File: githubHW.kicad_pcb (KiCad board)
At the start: 2 copper layers, 100.1 x 99.6 mm, 142 parts, among them J1 Conn_01x06, J2 Conn_01x07, J3 Conn_01x07, J4 Conn_01x07, J5 Conn_01x07, J6 Conn_01x06, SW1 SW_Push, SW2 SW_Push, SW3 SW_Push, SW4 SW_Push, U1 WeMos_mini, U2 TPIC6B595N, U3 TLC5940NT, U4 TPIC6B595N

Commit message: connection issue fixed
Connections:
- U4 pad 14: Net-(D101-Pad1) -> Net-(D103-Pad1)
- U4 pad 15: Net-(D100-Pad1) -> Net-(D104-Pad1)
- U4 pad 16: Net-(D106-Pad1) -> Net-(D105-Pad1)
- U4 pad 4: Net-(D105-Pad1) -> Net-(D106-Pad1)
- U4 pad 5: Net-(D104-Pad1) -> Net-(D100-Pad1)
- U4 pad 6: Net-(D103-Pad1) -> Net-(D101-Pad1)
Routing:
- net Net-(D103-Pad1): track 244.8 -> 271.5 mm
- net Net-(D104-Pad1): track 236.5 -> 260.0 mm
- net Net-(D105-Pad1): track 233.9 -> 255.1 mm
- net Net-(D101-Pad1): track 272.0 -> 257.5 mm
- net Net-(D100-Pad1): track 272.7 -> 259.0 mm
- net Net-(D106-Pad1): track 270.2 -> 257.5 mm
- net Net-(D100-Pad2): track 60.9 -> 62.7 mm
- net Net-(D92-Pad2): track 58.8 -> 60.5 mm

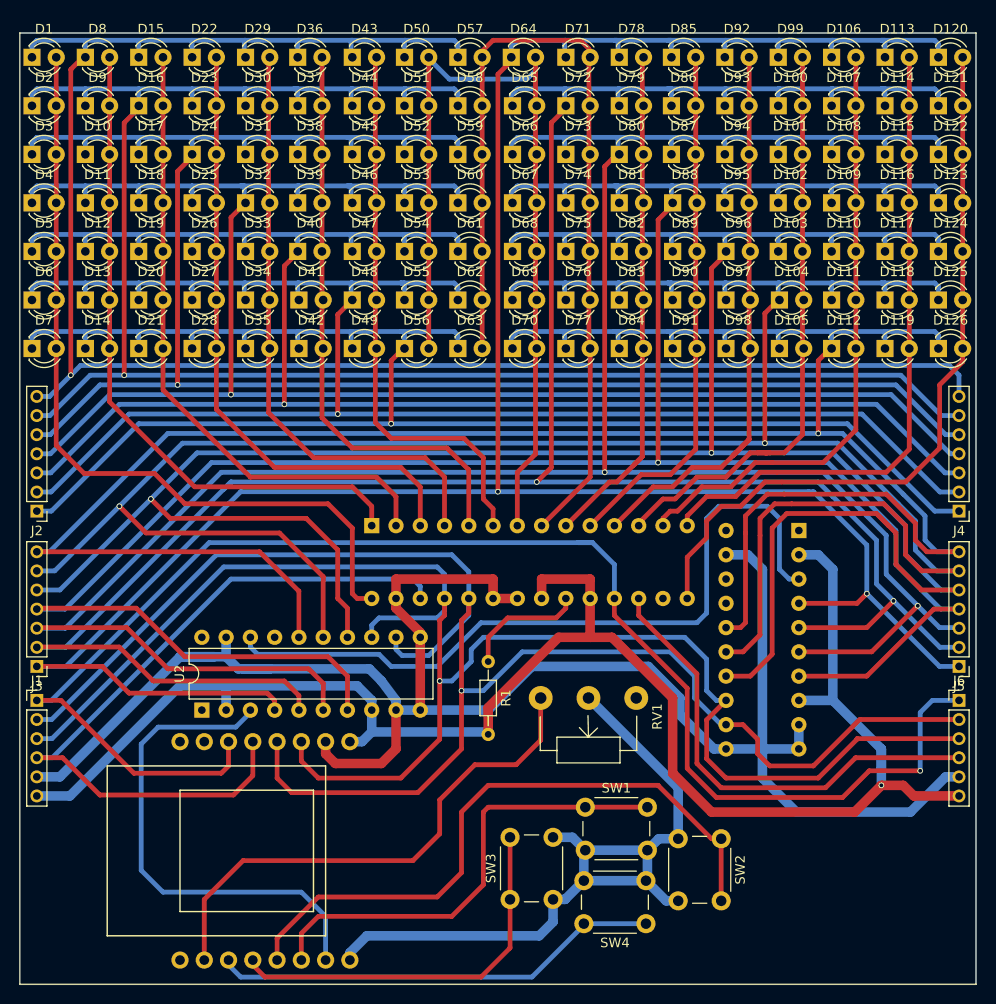
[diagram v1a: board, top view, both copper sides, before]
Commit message: buttons connection changed
now using WeMos' pullups
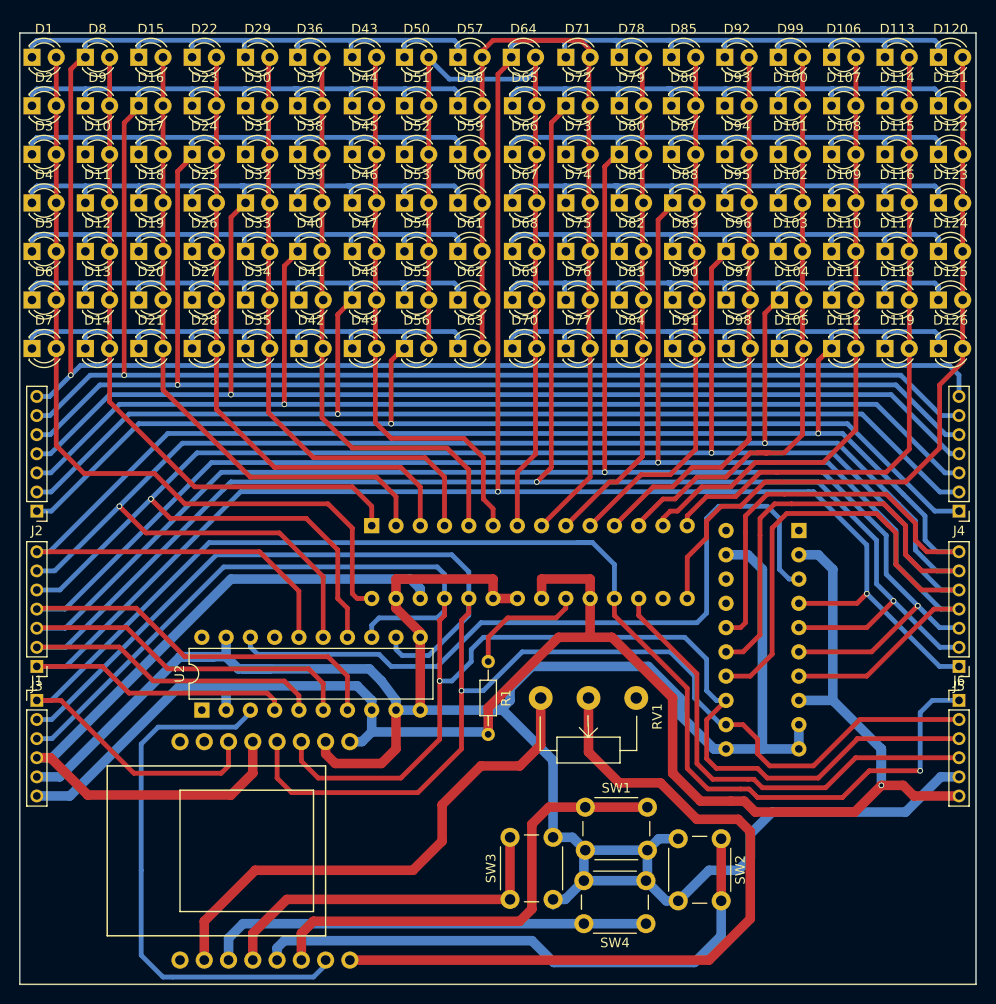
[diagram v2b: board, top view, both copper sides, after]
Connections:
- SW1 pad 2: /3.3V -> GND
- SW2 pad 2: /3.3V -> GND
- SW3 pad 2: /3.3V -> GND
- SW4 pad 2: /3.3V -> GND
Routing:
- net GND: track 198.8 -> 263.8 mm
- net Net-(SW2-Pad1): track 67.9 -> 60.3 mm
- net Net-(U1-Pad15): track 52.6 -> 56.9 mm
- net Net-(SW3-Pad1): track 40.8 -> 37.7 mm
- net /3.3V: track 81.9 -> 78.9 mm
- net Net-(RV1-Pad3): track 55.0 -> 54.1 mm
- net Net-(SW1-Pad1): track 48.9 -> 49.7 mm

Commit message: Revert "connection issue fixed"
This reverts commit d7eb6beb1c8d570a5e8c06e88c024579e6cb722b.
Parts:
- U4: moved to F.Cu
- moved U4 23.5 mm to (183.0, 150.2)
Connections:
- U4 pad 14: Net-(D103-Pad1) -> Net-(D10-Pad1)
- U4 pad 15: Net-(D104-Pad1) -> Net-(D16-Pad1)
- U4 pad 16: Net-(D105-Pad1) -> Net-(D1-Pad1)
- U4 pad 4: Net-(D106-Pad1) -> Net-(D14-Pad1)
- U4 pad 5: Net-(D100-Pad1) -> Net-(D13-Pad1)
- U4 pad 6: Net-(D101-Pad1) -> Net-(D12-Pad1)
- U4 pad 7: Net-(D102-Pad1) -> Net-(D11-Pad1)
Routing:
- net Net-(D103-Pad1): track 271.5 -> 224.6 mm
- net Net-(D1-Pad1): track 195.9 -> 240.9 mm
- net Net-(D104-Pad1): track 260.0 -> 216.8 mm
- net Net-(D105-Pad1): track 255.1 -> 213.6 mm
- net Net-(D16-Pad1): track 190.0 -> 230.5 mm
- net Net-(D10-Pad1): track 187.4 -> 219.9 mm
- net Net-(D14-Pad1): track 173.4 -> 198.3 mm
- net Net-(D13-Pad1): track 176.7 -> 201.6 mm
- net Net-(D12-Pad1): track 180.1 -> 204.6 mm
- net Net-(D11-Pad1): track 184.1 -> 207.4 mm
- net /M_CLK: track 172.5 -> 193.5 mm, vias 1 -> 3
- net Net-(D102-Pad1): track 260.3 -> 240.0 mm
- net Net-(D101-Pad1): track 257.5 -> 242.2 mm, vias 2 -> 1
- net /LATCH: track 174.0 -> 188.5 mm, vias 1 -> 4
- net Net-(D100-Pad1): track 259.0 -> 246.8 mm, vias 2 -> 1
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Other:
- net class Default: clearance 0.25 -> 0.3
- rule trace_clearance: 0.25 -> 0.3

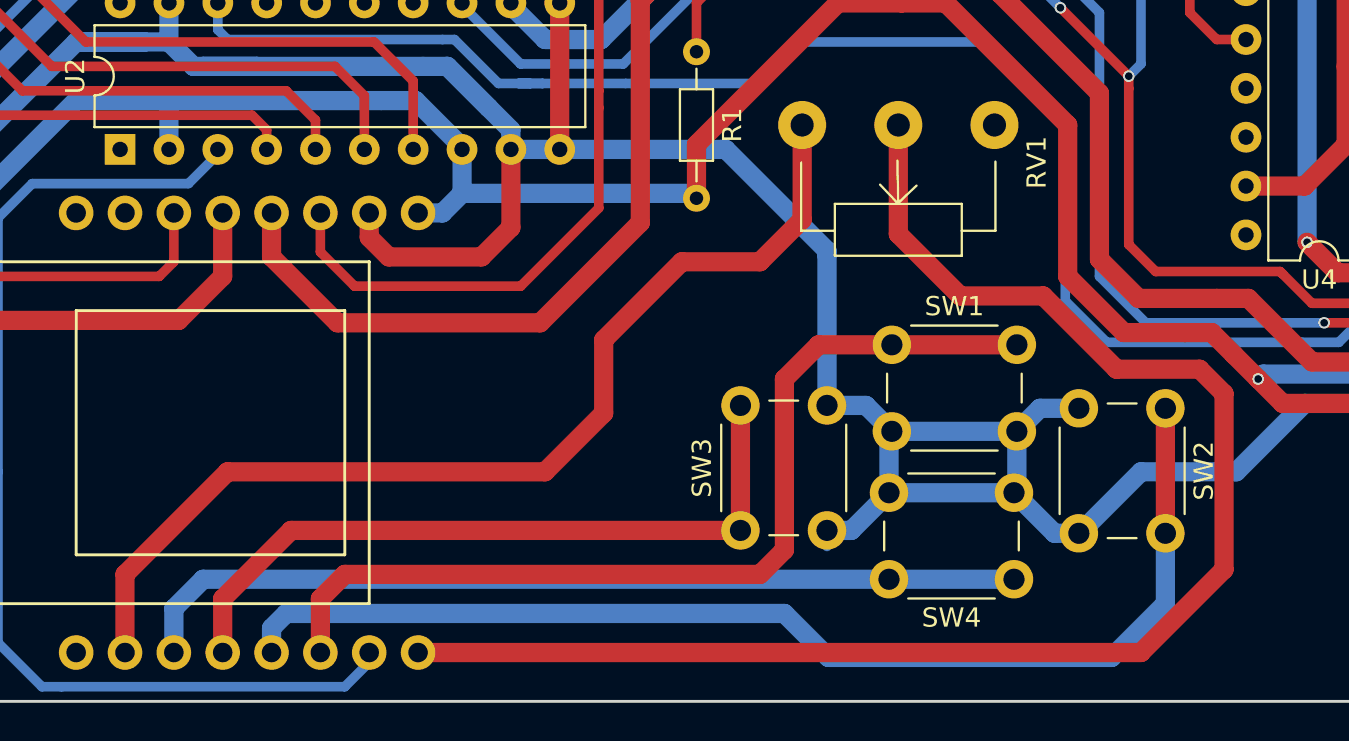
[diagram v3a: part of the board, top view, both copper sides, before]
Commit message: poti connection corrected
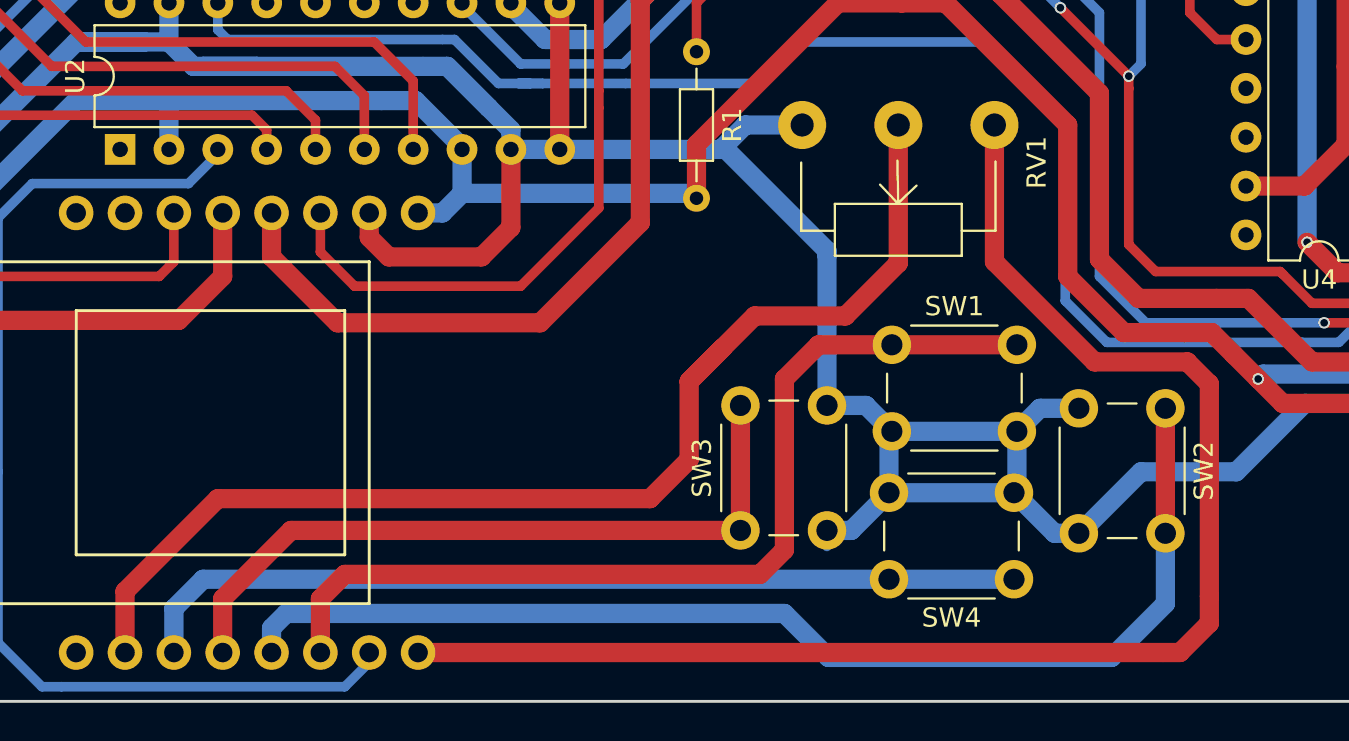
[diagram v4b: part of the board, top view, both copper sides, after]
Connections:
- RV1 pad 1: Net-(RV1-Pad1) -> /3.3V
- RV1 pad 2: /3.3V -> Net-(RV1-Pad2)
- RV1 pad 3: Net-(RV1-Pad3) -> GND
- U1 pad 10: Net-(RV1-Pad3) -> Net-(RV1-Pad2)
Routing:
- net Net-(RV1-Pad2): track 0.00 -> 63.0 mm
- net Net-(RV1-Pad3): track 54.1 -> 0.00 mm
- net GND: track 263.1 -> 267.9 mm
- net /3.3V: track 78.9 -> 75.1 mm

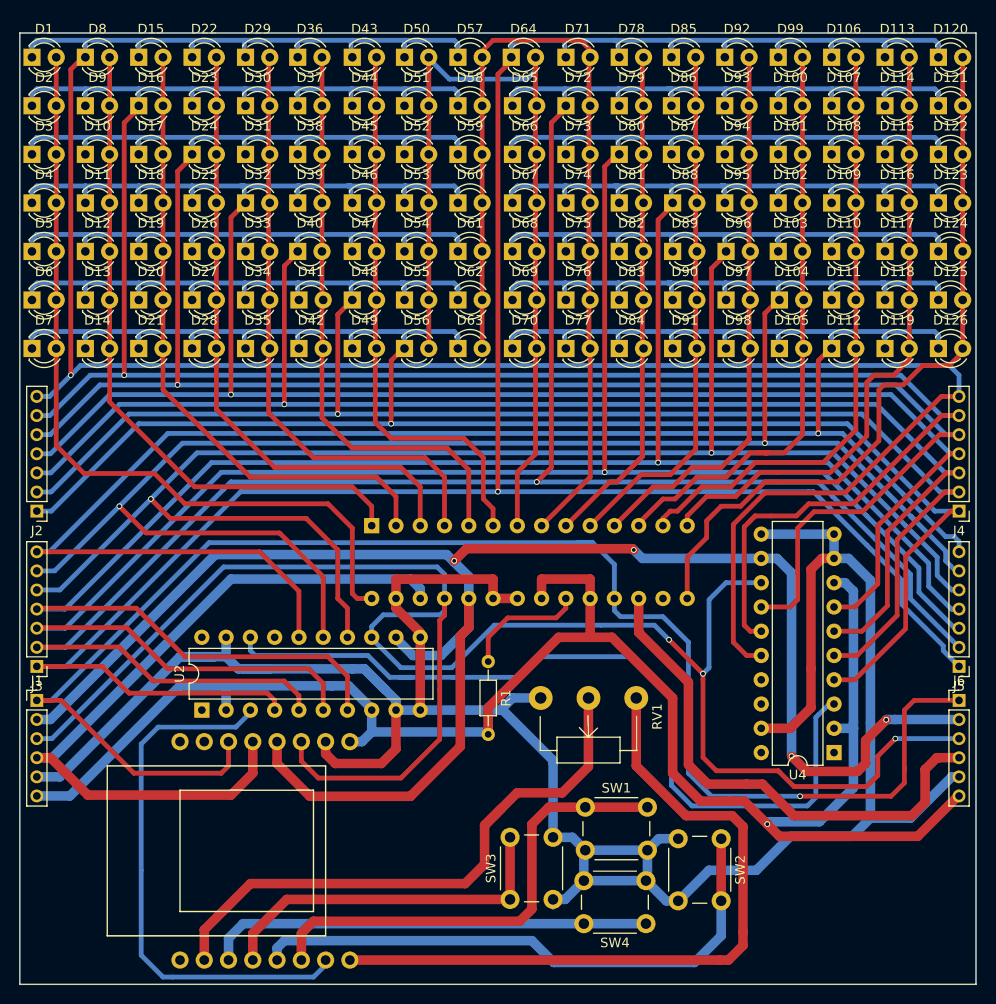
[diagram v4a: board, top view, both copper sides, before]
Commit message: wemos files commited for better usability.
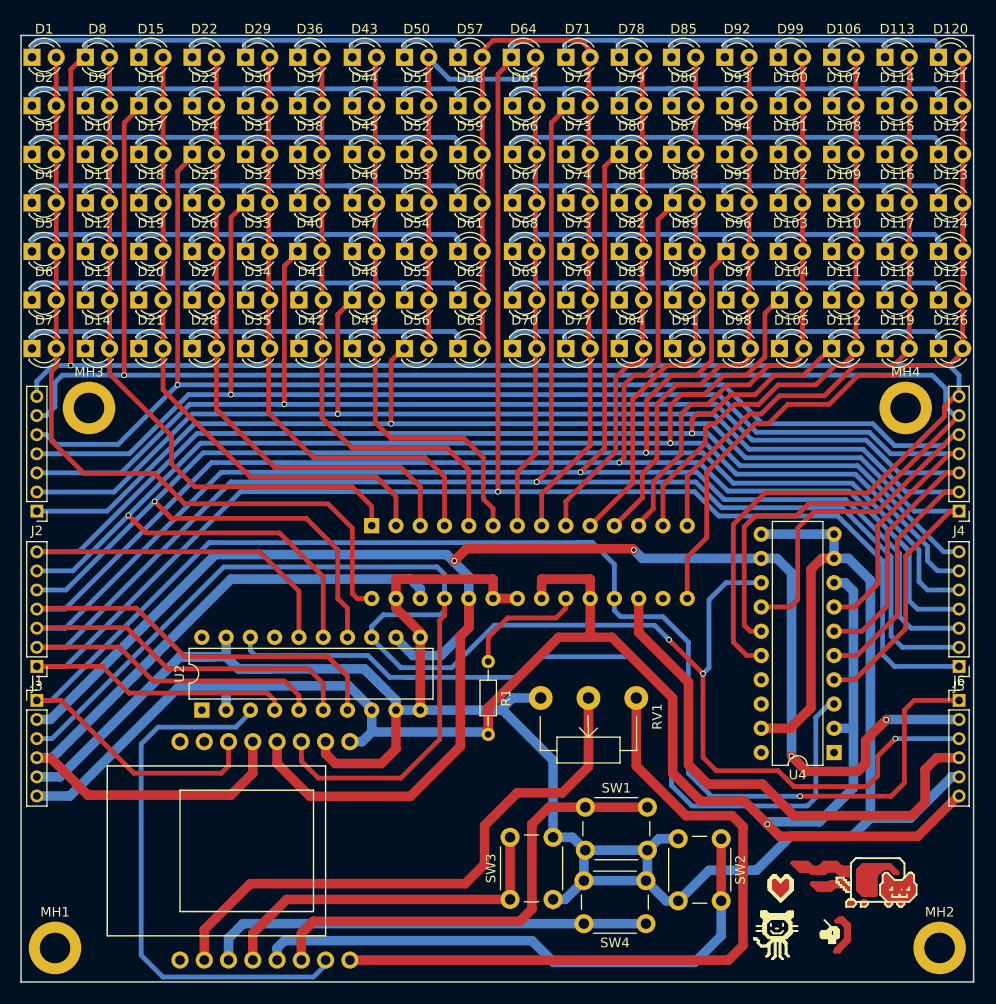
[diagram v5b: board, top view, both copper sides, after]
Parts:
- added MH1: MOUNTHOLE, Mounting_Holes:MountingHole_3.2mm_M3_ISO14580_Pad, F.Cu at (101.5, 170.7)
- added MH2: MOUNTHOLE, Mounting_Holes:MountingHole_3.2mm_M3_ISO14580_Pad, F.Cu at (194.1, 170.7)
- added MH3: MOUNTHOLE, Mounting_Holes:MountingHole_3.2mm_M3_ISO14580_Pad, F.Cu at (105.0, 114.2)
- added MH4: MOUNTHOLE, Mounting_Holes:MountingHole_3.2mm_M3_ISO14580_Pad, F.Cu at (190.5, 114.2)
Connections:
- D1 pad 1: Net-(D1-Pad1) -> Net-
- D1 pad 2: Net-(D1-Pad2) -> Net-
- D10 pad 1: Net-(D10-Pad1) -> Net-
- D10 pad 2: Net-(D10-Pad2) -> Net-
- D100 pad 1: Net-(D100-Pad1) -> Net-
- D100 pad 2: Net-(D100-Pad2) -> Net-
- D101 pad 1: Net-(D101-Pad1) -> Net-
- D101 pad 2: Net-(D100-Pad2) -> Net-
- D102 pad 1: Net-(D102-Pad1) -> Net-
- D102 pad 2: Net-(D100-Pad2) -> Net-
- D103 pad 1: Net-(D103-Pad1) -> Net-
- D103 pad 2: Net-(D100-Pad2) -> Net-
- D104 pad 1: Net-(D104-Pad1) -> Net-
- D104 pad 2: Net-(D100-Pad2) -> Net-
- D105 pad 1: Net-(D105-Pad1) -> Net-
- D105 pad 2: Net-(D100-Pad2) -> Net-
- D106 pad 1: Net-(D106-Pad1) -> Net-
- D106 pad 2: Net-(D106-Pad2) -> Net-
- D107 pad 1: Net-(D100-Pad1) -> Net-
- D107 pad 2: Net-(D106-Pad2) -> Net-
- D108 pad 1: Net-(D101-Pad1) -> Net-
- D108 pad 2: Net-(D106-Pad2) -> Net-
- D109 pad 1: Net-(D102-Pad1) -> Net-
- D109 pad 2: Net-(D106-Pad2) -> Net-
- D11 pad 1: Net-(D11-Pad1) -> Net-
- D11 pad 2: Net-(D10-Pad2) -> Net-
- D110 pad 1: Net-(D103-Pad1) -> Net-
- D110 pad 2: Net-(D106-Pad2) -> Net-
- D111 pad 1: Net-(D104-Pad1) -> Net-
- D111 pad 2: Net-(D106-Pad2) -> Net-
- D112 pad 1: Net-(D105-Pad1) -> Net-
- D112 pad 2: Net-(D106-Pad2) -> Net-
- D113 pad 1: Net-(D106-Pad1) -> Net-
- D113 pad 2: Net-(D113-Pad2) -> Net-
- D114 pad 1: Net-(D100-Pad1) -> Net-
- D114 pad 2: Net-(D113-Pad2) -> Net-
- D115 pad 1: Net-(D101-Pad1) -> Net-
- D115 pad 2: Net-(D113-Pad2) -> Net-
- D116 pad 1: Net-(D102-Pad1) -> Net-
- D116 pad 2: Net-(D113-Pad2) -> Net-
- D117 pad 1: Net-(D103-Pad1) -> Net-
- D117 pad 2: Net-(D113-Pad2) -> Net-
- D118 pad 1: Net-(D104-Pad1) -> Net-
- D118 pad 2: Net-(D113-Pad2) -> Net-
- D119 pad 1: Net-(D105-Pad1) -> Net-
- D119 pad 2: Net-(D113-Pad2) -> Net-
- D12 pad 1: Net-(D12-Pad1) -> Net-
- D12 pad 2: Net-(D10-Pad2) -> Net-
- D120 pad 1: Net-(D106-Pad1) -> Net-
- D120 pad 2: Net-(D120-Pad2) -> Net-
- D121 pad 1: Net-(D100-Pad1) -> Net-
- D121 pad 2: Net-(D120-Pad2) -> Net-
- D122 pad 1: Net-(D101-Pad1) -> Net-
- D122 pad 2: Net-(D120-Pad2) -> Net-
- D123 pad 1: Net-(D102-Pad1) -> Net-
- D123 pad 2: Net-(D120-Pad2) -> Net-
- D124 pad 1: Net-(D103-Pad1) -> Net-
- D124 pad 2: Net-(D120-Pad2) -> Net-
- D125 pad 1: Net-(D104-Pad1) -> Net-
- D125 pad 2: Net-(D120-Pad2) -> Net-
- D126 pad 1: Net-(D105-Pad1) -> Net-
- D126 pad 2: Net-(D120-Pad2) -> Net-
- D13 pad 1: Net-(D13-Pad1) -> Net-
- D13 pad 2: Net-(D10-Pad2) -> Net-
- D14 pad 1: Net-(D14-Pad1) -> Net-
- D14 pad 2: Net-(D10-Pad2) -> Net-
- D15 pad 1: Net-(D1-Pad1) -> Net-
- D15 pad 2: Net-(D15-Pad2) -> Net-
- D16 pad 1: Net-(D16-Pad1) -> Net-
- D16 pad 2: Net-(D15-Pad2) -> Net-
- D17 pad 1: Net-(D10-Pad1) -> Net-
- D17 pad 2: Net-(D15-Pad2) -> Net-
- D18 pad 1: Net-(D11-Pad1) -> Net-
- D18 pad 2: Net-(D15-Pad2) -> Net-
- D19 pad 1: Net-(D12-Pad1) -> Net-
- D19 pad 2: Net-(D15-Pad2) -> Net-
- D2 pad 1: Net-(D16-Pad1) -> Net-
- D2 pad 2: Net-(D1-Pad2) -> Net-
- D20 pad 1: Net-(D13-Pad1) -> Net-
- D20 pad 2: Net-(D15-Pad2) -> Net-
- D21 pad 1: Net-(D14-Pad1) -> Net-
- D21 pad 2: Net-(D15-Pad2) -> Net-
- D22 pad 1: Net-(D1-Pad1) -> Net-
- D22 pad 2: Net-(D22-Pad2) -> Net-
- D23 pad 1: Net-(D16-Pad1) -> Net-
- D23 pad 2: Net-(D22-Pad2) -> Net-
- D24 pad 1: Net-(D10-Pad1) -> Net-
- D24 pad 2: Net-(D22-Pad2) -> Net-
- D25 pad 1: Net-(D11-Pad1) -> Net-
- D25 pad 2: Net-(D22-Pad2) -> Net-
- D26 pad 1: Net-(D12-Pad1) -> Net-
- D26 pad 2: Net-(D22-Pad2) -> Net-
- D27 pad 1: Net-(D13-Pad1) -> Net-
- D27 pad 2: Net-(D22-Pad2) -> Net-
- D28 pad 1: Net-(D14-Pad1) -> Net-
- D28 pad 2: Net-(D22-Pad2) -> Net-
- D29 pad 1: Net-(D1-Pad1) -> Net-
- D29 pad 2: Net-(D29-Pad2) -> Net-
- D3 pad 1: Net-(D10-Pad1) -> Net-
- D3 pad 2: Net-(D1-Pad2) -> Net-
- D30 pad 1: Net-(D16-Pad1) -> Net-
- D30 pad 2: Net-(D29-Pad2) -> Net-
- D31 pad 1: Net-(D10-Pad1) -> Net-
- D31 pad 2: Net-(D29-Pad2) -> Net-
- D32 pad 1: Net-(D11-Pad1) -> Net-
- D32 pad 2: Net-(D29-Pad2) -> Net-
- D33 pad 1: Net-(D12-Pad1) -> Net-
- D33 pad 2: Net-(D29-Pad2) -> Net-
- D34 pad 1: Net-(D13-Pad1) -> Net-
- D34 pad 2: Net-(D29-Pad2) -> Net-
- D35 pad 1: Net-(D14-Pad1) -> Net-
- D35 pad 2: Net-(D29-Pad2) -> Net-
- D36 pad 1: Net-(D1-Pad1) -> Net-
- D36 pad 2: Net-(D36-Pad2) -> Net-
- D37 pad 1: Net-(D16-Pad1) -> Net-
- D37 pad 2: Net-(D36-Pad2) -> Net-
- D38 pad 1: Net-(D10-Pad1) -> Net-
- D38 pad 2: Net-(D36-Pad2) -> Net-
- D39 pad 1: Net-(D11-Pad1) -> Net-
- D39 pad 2: Net-(D36-Pad2) -> Net-
- D4 pad 1: Net-(D11-Pad1) -> Net-
- D4 pad 2: Net-(D1-Pad2) -> Net-
- D40 pad 1: Net-(D12-Pad1) -> Net-
- D40 pad 2: Net-(D36-Pad2) -> Net-
- D41 pad 1: Net-(D13-Pad1) -> Net-
- D41 pad 2: Net-(D36-Pad2) -> Net-
- D42 pad 1: Net-(D14-Pad1) -> Net-
- D42 pad 2: Net-(D36-Pad2) -> Net-
- D43 pad 1: Net-(D1-Pad1) -> Net-
- D43 pad 2: Net-(D43-Pad2) -> Net-
- D44 pad 1: Net-(D16-Pad1) -> Net-
- D44 pad 2: Net-(D43-Pad2) -> Net-
- D45 pad 1: Net-(D10-Pad1) -> Net-
- D45 pad 2: Net-(D43-Pad2) -> Net-
- D46 pad 1: Net-(D11-Pad1) -> Net-
- D46 pad 2: Net-(D43-Pad2) -> Net-
- D47 pad 1: Net-(D12-Pad1) -> Net-
- D47 pad 2: Net-(D43-Pad2) -> Net-
- D48 pad 1: Net-(D13-Pad1) -> Net-
- D48 pad 2: Net-(D43-Pad2) -> Net-
- D49 pad 1: Net-(D14-Pad1) -> Net-
- D49 pad 2: Net-(D43-Pad2) -> Net-
- D5 pad 1: Net-(D12-Pad1) -> Net-
- D5 pad 2: Net-(D1-Pad2) -> Net-
- D50 pad 1: Net-(D1-Pad1) -> Net-
- D50 pad 2: Net-(D50-Pad2) -> Net-
- D51 pad 1: Net-(D16-Pad1) -> Net-
- D51 pad 2: Net-(D50-Pad2) -> Net-
- D52 pad 1: Net-(D10-Pad1) -> Net-
- D52 pad 2: Net-(D50-Pad2) -> Net-
- D53 pad 1: Net-(D11-Pad1) -> Net-
- D53 pad 2: Net-(D50-Pad2) -> Net-
- D54 pad 1: Net-(D12-Pad1) -> Net-
- D54 pad 2: Net-(D50-Pad2) -> Net-
- D55 pad 1: Net-(D13-Pad1) -> Net-
- D55 pad 2: Net-(D50-Pad2) -> Net-
- D56 pad 1: Net-(D14-Pad1) -> Net-
- D56 pad 2: Net-(D50-Pad2) -> Net-
- D57 pad 1: Net-(D1-Pad1) -> Net-
- D57 pad 2: Net-(D57-Pad2) -> Net-
- D58 pad 1: Net-(D16-Pad1) -> Net-
- D58 pad 2: Net-(D57-Pad2) -> Net-
- D59 pad 1: Net-(D10-Pad1) -> Net-
- D59 pad 2: Net-(D57-Pad2) -> Net-
- D6 pad 1: Net-(D13-Pad1) -> Net-
- D6 pad 2: Net-(D1-Pad2) -> Net-
- D60 pad 1: Net-(D11-Pad1) -> Net-
- D60 pad 2: Net-(D57-Pad2) -> Net-
- D61 pad 1: Net-(D12-Pad1) -> Net-
- D61 pad 2: Net-(D57-Pad2) -> Net-
- D62 pad 1: Net-(D13-Pad1) -> Net-
- D62 pad 2: Net-(D57-Pad2) -> Net-
- D63 pad 1: Net-(D14-Pad1) -> Net-
- D63 pad 2: Net-(D57-Pad2) -> Net-
- D64 pad 1: Net-(D106-Pad1) -> Net-
- D64 pad 2: Net-(D50-Pad2) -> Net-
- D65 pad 1: Net-(D100-Pad1) -> Net-
- D65 pad 2: Net-(D50-Pad2) -> Net-
- D66 pad 1: Net-(D101-Pad1) -> Net-
- D66 pad 2: Net-(D50-Pad2) -> Net-
- D67 pad 1: Net-(D102-Pad1) -> Net-
- D67 pad 2: Net-(D50-Pad2) -> Net-
- D68 pad 1: Net-(D103-Pad1) -> Net-
- D68 pad 2: Net-(D50-Pad2) -> Net-
- D69 pad 1: Net-(D104-Pad1) -> Net-
- D69 pad 2: Net-(D50-Pad2) -> Net-
- D7 pad 1: Net-(D14-Pad1) -> Net-
- D7 pad 2: Net-(D1-Pad2) -> Net-
- D70 pad 1: Net-(D105-Pad1) -> Net-
- D70 pad 2: Net-(D50-Pad2) -> Net-
- D71 pad 1: Net-(D106-Pad1) -> Net-
- D71 pad 2: Net-(D57-Pad2) -> Net-
- D72 pad 1: Net-(D100-Pad1) -> Net-
- D72 pad 2: Net-(D57-Pad2) -> Net-
- D73 pad 1: Net-(D101-Pad1) -> Net-
- D73 pad 2: Net-(D57-Pad2) -> Net-
- D74 pad 1: Net-(D102-Pad1) -> Net-
- D74 pad 2: Net-(D57-Pad2) -> Net-
- D75 pad 1: Net-(D103-Pad1) -> Net-
- D75 pad 2: Net-(D57-Pad2) -> Net-
- D76 pad 1: Net-(D104-Pad1) -> Net-
- D76 pad 2: Net-(D57-Pad2) -> Net-
- D77 pad 1: Net-(D105-Pad1) -> Net-
- D77 pad 2: Net-(D57-Pad2) -> Net-
- D78 pad 1: Net-(D106-Pad1) -> Net-
- D78 pad 2: Net-(D78-Pad2) -> Net-
- D79 pad 1: Net-(D100-Pad1) -> Net-
- D79 pad 2: Net-(D78-Pad2) -> Net-
- D8 pad 1: Net-(D1-Pad1) -> Net-
- D8 pad 2: Net-(D10-Pad2) -> Net-
- D80 pad 1: Net-(D101-Pad1) -> Net-
- D80 pad 2: Net-(D78-Pad2) -> Net-
- D81 pad 1: Net-(D102-Pad1) -> Net-
- D81 pad 2: Net-(D78-Pad2) -> Net-
- D82 pad 1: Net-(D103-Pad1) -> Net-
- D82 pad 2: Net-(D78-Pad2) -> Net-
- D83 pad 1: Net-(D104-Pad1) -> Net-
- D83 pad 2: Net-(D78-Pad2) -> Net-
- D84 pad 1: Net-(D105-Pad1) -> Net-
- D84 pad 2: Net-(D78-Pad2) -> Net-
- D85 pad 1: Net-(D106-Pad1) -> Net-
- D85 pad 2: Net-(D85-Pad2) -> Net-
- D86 pad 1: Net-(D100-Pad1) -> Net-
- D86 pad 2: Net-(D85-Pad2) -> Net-
- D87 pad 1: Net-(D101-Pad1) -> Net-
- D87 pad 2: Net-(D85-Pad2) -> Net-
- D88 pad 1: Net-(D102-Pad1) -> Net-
- D88 pad 2: Net-(D85-Pad2) -> Net-
- D89 pad 1: Net-(D103-Pad1) -> Net-
- D89 pad 2: Net-(D85-Pad2) -> Net-
- D9 pad 1: Net-(D16-Pad1) -> Net-
- D9 pad 2: Net-(D10-Pad2) -> Net-
- D90 pad 1: Net-(D104-Pad1) -> Net-
- D90 pad 2: Net-(D85-Pad2) -> Net-
- D91 pad 1: Net-(D105-Pad1) -> Net-
- D91 pad 2: Net-(D85-Pad2) -> Net-
- D92 pad 1: Net-(D106-Pad1) -> Net-
- D92 pad 2: Net-(D92-Pad2) -> Net-
- D93 pad 1: Net-(D100-Pad1) -> Net-
- D93 pad 2: Net-(D92-Pad2) -> Net-
- D94 pad 1: Net-(D101-Pad1) -> Net-
- D94 pad 2: Net-(D92-Pad2) -> Net-
- D95 pad 1: Net-(D102-Pad1) -> Net-
- D95 pad 2: Net-(D92-Pad2) -> Net-
- D96 pad 1: Net-(D103-Pad1) -> Net-
- D96 pad 2: Net-(D92-Pad2) -> Net-
- D97 pad 1: Net-(D104-Pad1) -> Net-
- D97 pad 2: Net-(D92-Pad2) -> Net-
- D98 pad 1: Net-(D105-Pad1) -> Net-
- D98 pad 2: Net-(D92-Pad2) -> Net-
- D99 pad 1: Net-(D106-Pad1) -> Net-
- D99 pad 2: Net-(D100-Pad2) -> Net-
- J1 pad 4: Net-(J1-Pad4) -> Net-
- J2 pad 1: Net-(D14-Pad1) -> Net-
- J2 pad 2: Net-(D13-Pad1) -> Net-
- J2 pad 3: Net-(D12-Pad1) -> Net-
- J2 pad 4: Net-(D11-Pad1) -> Net-
- J2 pad 5: Net-(D10-Pad1) -> Net-
- J2 pad 6: Net-(D16-Pad1) -> Net-
- J2 pad 7: Net-(D1-Pad1) -> Net-
- J3 pad 1: Net-(D106-Pad1) -> Net-
- J3 pad 2: Net-(D100-Pad1) -> Net-
- J3 pad 3: Net-(D101-Pad1) -> Net-
- J3 pad 4: Net-(D102-Pad1) -> Net-
- J3 pad 5: Net-(D103-Pad1) -> Net-
- J3 pad 6: Net-(D104-Pad1) -> Net-
- J3 pad 7: Net-(D105-Pad1) -> Net-
- J4 pad 1: Net-(D14-Pad1) -> Net-
- J4 pad 2: Net-(D13-Pad1) -> Net-
- J4 pad 3: Net-(D12-Pad1) -> Net-
- J4 pad 4: Net-(D11-Pad1) -> Net-
- J4 pad 5: Net-(D10-Pad1) -> Net-
- J4 pad 6: Net-(D16-Pad1) -> Net-
- J4 pad 7: Net-(D1-Pad1) -> Net-
- J5 pad 1: Net-(D106-Pad1) -> Net-
- J5 pad 2: Net-(D100-Pad1) -> Net-
- J5 pad 3: Net-(D101-Pad1) -> Net-
- J5 pad 4: Net-(D102-Pad1) -> Net-
- J5 pad 5: Net-(D103-Pad1) -> Net-
- J5 pad 6: Net-(D104-Pad1) -> Net-
- J5 pad 7: Net-(D105-Pad1) -> Net-
- J6 pad 4: Net-(J6-Pad4) -> Net-
- R1 pad 1: Net-(R1-Pad1) -> Net-
- RV1 pad 2: Net-(RV1-Pad2) -> Net-
- SW1 pad 1: Net-(SW1-Pad1) -> Net-
- SW2 pad 1: Net-(SW2-Pad1) -> Net-
- SW3 pad 1: Net-(SW3-Pad1) -> Net-
- SW4 pad 1: Net-(SW4-Pad1) -> Net-
- U1 pad 10: Net-(RV1-Pad2) -> Net-
- U1 pad 11: Net-(SW4-Pad1) -> Net-
- U1 pad 12: Net-(SW3-Pad1) -> Net-
- U1 pad 13: Net-(SW2-Pad1) -> Net-
- U1 pad 14: Net-(SW1-Pad1) -> Net-
- U1 pad 15: Net-(U1-Pad15) -> Net-
- U1 pad 5: Net-(J1-Pad4) -> Net-
- U1 pad 7: Net-(U1-Pad7) -> (no net)
- U1 pad 8: Net-(U1-Pad8) -> (no net)
- U1 pad 9: Net-(U1-Pad9) -> (no net)
- U2 pad 1: Net-(U2-Pad1) -> (no net)
- U2 pad 14: Net-(D103-Pad1) -> Net-
- U2 pad 15: Net-(D104-Pad1) -> Net-
- U2 pad 16: Net-(D105-Pad1) -> Net-
- U2 pad 17: Net-(U2-Pad17) -> (no net)
- U2 pad 18: Net-(U2-Pad18) -> Net-
- U2 pad 20: Net-(U2-Pad20) -> (no net)
- U2 pad 3: Net-(U1-Pad15) -> Net-
- U2 pad 4: Net-(D106-Pad1) -> Net-
- U2 pad 5: Net-(D100-Pad1) -> Net-
- U2 pad 6: Net-(D101-Pad1) -> Net-
- U2 pad 7: Net-(D102-Pad1) -> Net-
- U3 pad 1: Net-(D10-Pad2) -> Net-
- U3 pad 10: Net-(D85-Pad2) -> Net-
- U3 pad 11: Net-(D92-Pad2) -> Net-
- U3 pad 12: Net-(D100-Pad2) -> Net-
- U3 pad 13: Net-(D106-Pad2) -> Net-
- U3 pad 14: Net-(D113-Pad2) -> Net-
- U3 pad 15: Net-(D120-Pad2) -> Net-
- U3 pad 16: Net-(U3-Pad16) -> (no net)
- U3 pad 17: Net-(J6-Pad4) -> Net-
- U3 pad 2: Net-(D15-Pad2) -> Net-
- U3 pad 20: Net-(R1-Pad1) -> Net-
- U3 pad 26: Net-(J1-Pad4) -> Net-
- U3 pad 28: Net-(D1-Pad2) -> Net-
- U3 pad 3: Net-(D22-Pad2) -> Net-
- U3 pad 4: Net-(D29-Pad2) -> Net-
- U3 pad 5: Net-(D36-Pad2) -> Net-
- U3 pad 6: Net-(D43-Pad2) -> Net-
- U3 pad 7: Net-(D50-Pad2) -> Net-
- U3 pad 8: Net-(D57-Pad2) -> Net-
- U3 pad 9: Net-(D78-Pad2) -> Net-
- U4 pad 1: Net-(U4-Pad1) -> (no net)
- U4 pad 14: Net-(D10-Pad1) -> Net-
- U4 pad 15: Net-(D16-Pad1) -> Net-
- U4 pad 16: Net-(D1-Pad1) -> Net-
- U4 pad 17: Net-(U4-Pad17) -> (no net)
- U4 pad 18: Net-(U4-Pad18) -> (no net)
- U4 pad 20: Net-(U4-Pad20) -> (no net)
- U4 pad 3: Net-(U2-Pad18) -> Net-
- U4 pad 4: Net-(D14-Pad1) -> Net-
- U4 pad 5: Net-(D13-Pad1) -> Net-
- U4 pad 6: Net-(D12-Pad1) -> Net-
- U4 pad 7: Net-(D11-Pad1) -> Net-
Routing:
- net Net-: track 0.00 -> 4818.2 mm, vias 0 -> 16
- net Net-(D106-Pad1): track 248.8 -> 0.00 mm, vias 1 -> 0
- net Net-(D100-Pad1): track 246.8 -> 0.00 mm, vias 1 -> 0
- net Net-(D101-Pad1): track 242.2 -> 0.00 mm, vias 1 -> 0
- net Net-(D1-Pad1): track 240.9 -> 0.00 mm, vias 1 -> 0
- net Net-(D102-Pad1): track 240.0 -> 0.00 mm, vias 1 -> 0
- net Net-(D16-Pad1): track 230.5 -> 0.00 mm, vias 1 -> 0
- net Net-(D103-Pad1): track 224.6 -> 0.00 mm, vias 2 -> 0
- net Net-(D10-Pad1): track 219.9 -> 0.00 mm, vias 1 -> 0
- net Net-(D104-Pad1): track 216.8 -> 0.00 mm, vias 2 -> 0
- net Net-(D105-Pad1): track 213.6 -> 0.00 mm, vias 1 -> 0
- net Net-(D11-Pad1): track 207.4 -> 0.00 mm, vias 1 -> 0
- net Net-(D12-Pad1): track 204.6 -> 0.00 mm, vias 1 -> 0
- net Net-(D13-Pad1): track 201.6 -> 0.00 mm, vias 1 -> 0
- net Net-(D14-Pad1): track 198.3 -> 0.00 mm, vias 1 -> 0
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- added copper zone on F.Cu, net (none)
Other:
- board size 100.1 x 99.6 mm -> 99.7 x 99.1 mm
